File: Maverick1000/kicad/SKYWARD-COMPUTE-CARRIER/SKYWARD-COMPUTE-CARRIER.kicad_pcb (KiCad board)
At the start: 4 copper layers, 110 x 125 mm, 118 parts, among them J1 CM4_J1, J10 DEBUG, J11 SIM_TRAY, J12 ANT_CELLULAR, J13 USB_BOOT, J2 CM4_J2, J3 BATT_IN, J4 DOCK, J5 FC, J6 GNSS, J7 ELRS, J8 TOF, J9 TERRA, Q1 DMP2305U-7, Q2 DMP2305U-7, Q5 DMP2305U-7, Q6 DMP2305U-7, SW1 nRPIBOOT, SW2 RUN, U1 LM74610QDGKRQ1, U10 FSUSB42MUX, U2 LM74610QDGKRQ1, U3 BQ25792RQMR, U4 TPS5430DDA, U5 AP2112K-3.3TRG1, U6 INA3221AIPW, U7 USB2512B-AEZG-TR, U8 EC25VFA-512-STD, U9 TPS5430DDA, Y1 24MHz

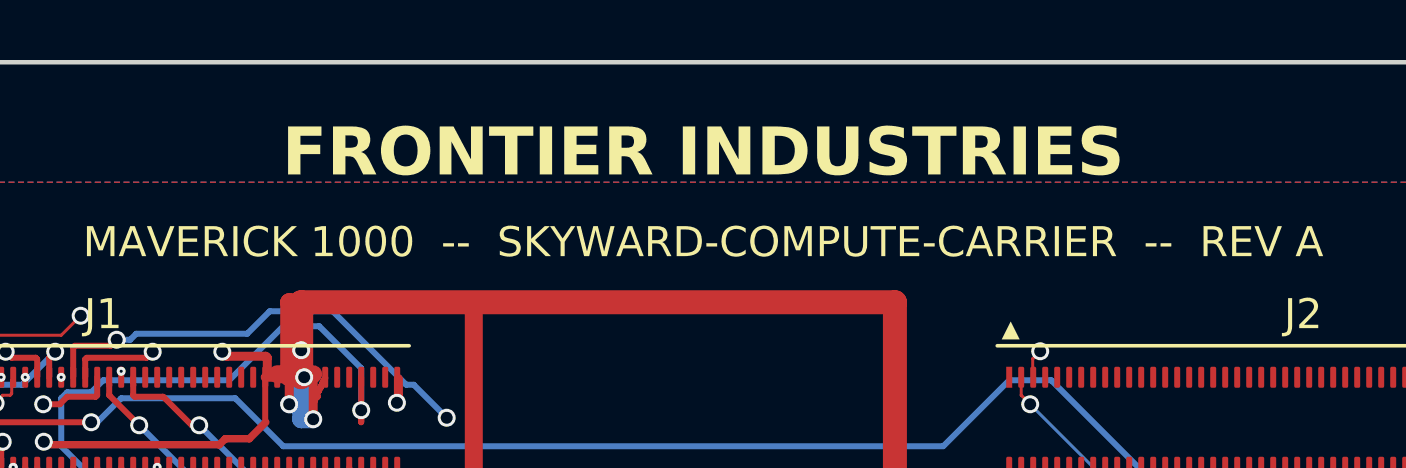
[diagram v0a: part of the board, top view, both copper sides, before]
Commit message: Rename company Frontier Robotics/Industries -> Frontier Innovations
Applied consistently across every instance: KiCad schematic/PCB source
(including the board's own silkscreen text and the three Python
generator scripts that produce it, so regeneration won't reintroduce
the old name), exported netlists, and docs. Re-verified after the
rename with real tooling, not just trusted:

- Re-rendered the board's silkscreen (kicad-cli, --exclude-drawing-
  sheet) and visually confirmed "FRONTIER INNOVATIONS" is centered and
  clear of the mounting-hole labels on both edges, no overflow.
- Re-ran python/run_drc.py: still 0 unconnected pads, same 2 pre-
  existing/documented lib_footprint_mismatch warnings, nothing new.
- Re-ran the netlist cross-check against a fresh kicad-cli export:
  still 0 mismatches, 469/469.
- Regenerated the two manufacturing preview SVGs that still had the
  old name baked into their rendered text.

Left one historical quote in docs/FINAL_DESIGN_AUDIT.md untouched
(a past session's note describing a stale "FRONTIER ROBOTICS" board
silkscreen bug it found and fixed) since rewriting it would make that
history inaccurate, not more correct.

Co-Authored-By: Claude Sonnet 5 <noreply@anthropic.com>
Claude-Session: https://claude.ai/code/session_01PjVLbuUxJUCeC3xm5gJT9X
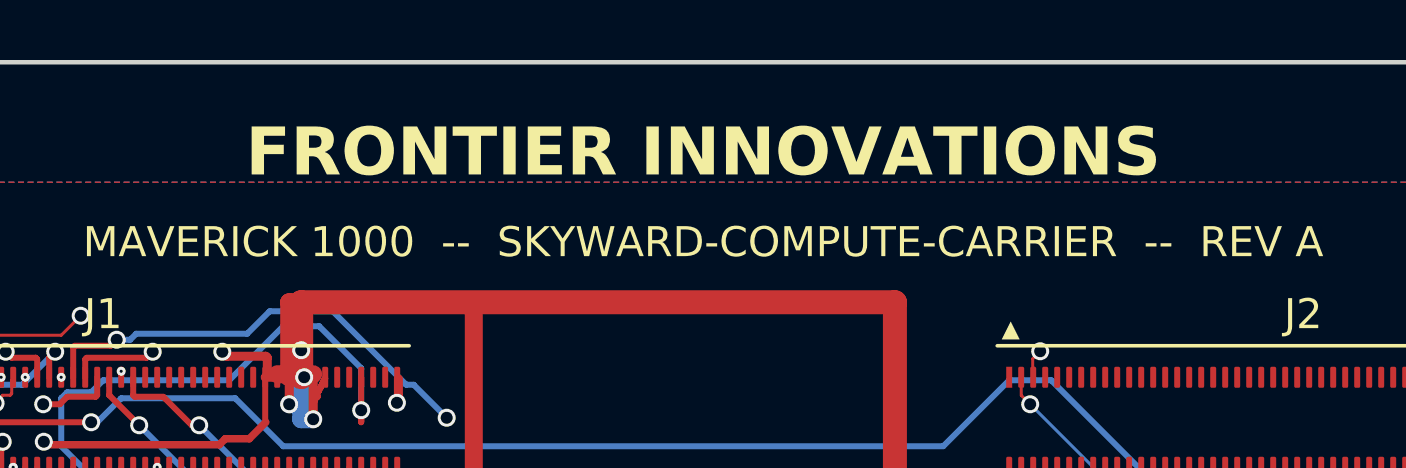
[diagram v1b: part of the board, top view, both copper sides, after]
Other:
- board text added: "FRONTIER INNOVATIONS"
- board text removed: "FRONTIER INDUSTRIES"
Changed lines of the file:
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@@
   (gr_line (start 0 0) (end 110 0)
     (stroke (width 0.15) (type default)) (layer "Edge.Cuts"))
-  (gr_text "FRONTIER INDUSTRIES" (at 55 3) (layer "F.SilkS")
+  (gr_text "FRONTIER INNOVATIONS" (at 55 3) (layer "F.SilkS")
     (effects (font (size 1.6 1.6) (thickness 0.15) bold))
   )
